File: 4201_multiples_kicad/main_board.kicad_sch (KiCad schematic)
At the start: 31 parts, among them J19 Conn_02x05_Odd_Even, U1 TL074, U2 TL074

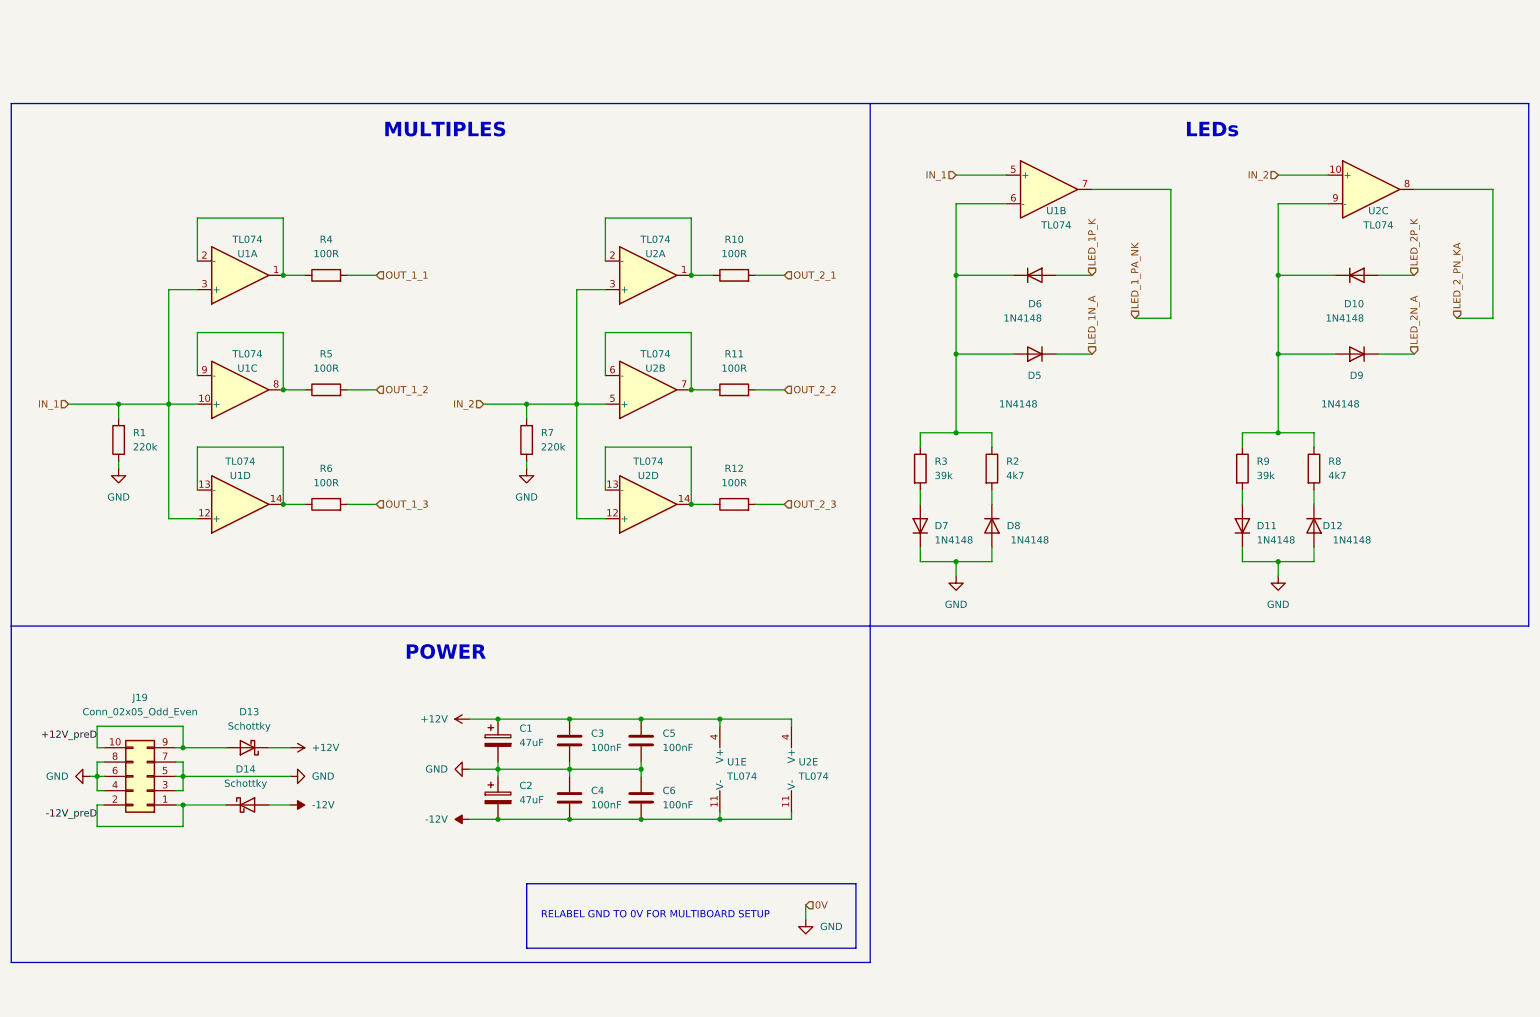
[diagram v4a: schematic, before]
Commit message: Update LED current limiting resistor values for equal brightness
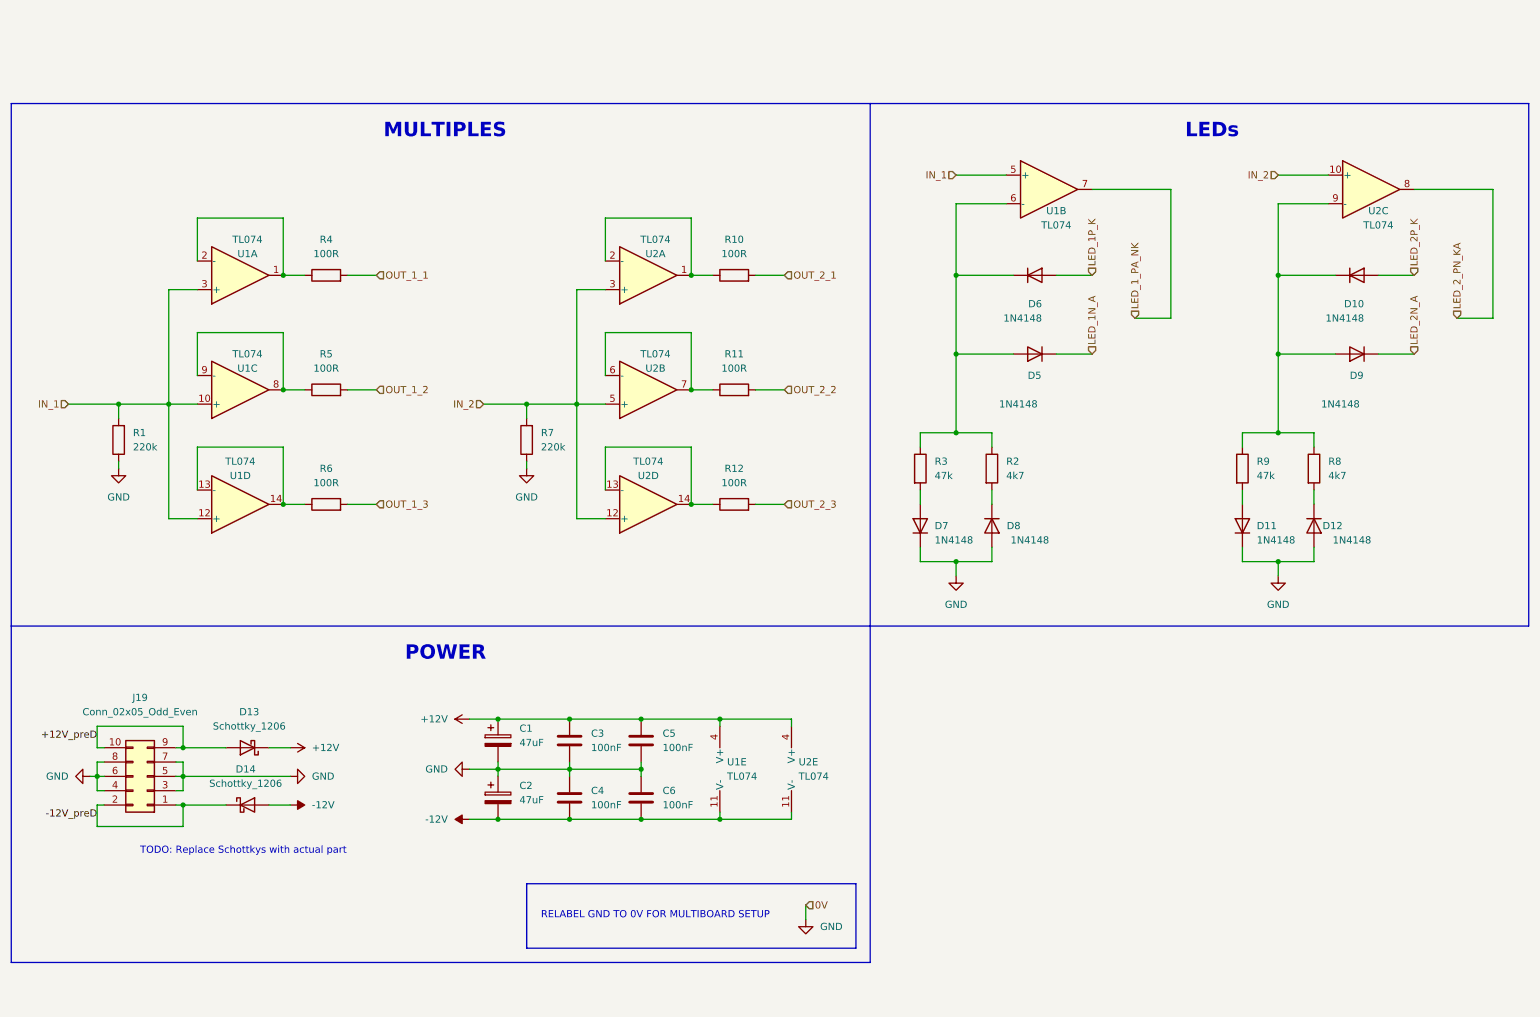
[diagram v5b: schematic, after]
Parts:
- D13, D14: value Schottky -> Schottky_1206
- R3, R9: value 39k -> 47k
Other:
- note added: "TODO: Replace Schottkys with actual part"
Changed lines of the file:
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@@
     (effects (font (size 2.54 2.54) bold) (justify left bottom))
+  )
+  (text "TODO: Replace Schottkys with actual part" (at 36.83 165.1 0)
+    (effects (font (size 1.27 1.27)) (justify left bottom))
   )
   (text "LEDs" (at 222.25 38.1 0)
@@
       (effects (font (size 1.27 1.27)) (justify left))
     )
-    (property "Value" "39k" (id 1) (at 177.8 97.7899 0)
+    (property "Value" "47k" (id 1) (at 177.8 97.7899 0)
       (effects (font (size 1.27 1.27)) (justify left))
     )
@@
     (in_bom yes) (on_board yes) (fields_autoplaced)
     (property "Reference" "D13" (id 0) (at 56.1975 139.7 0))
-    (property "Value" "Schottky" (id 1) (at 56.1975 142.24 0))
+    (property "Value" "Schottky_1206" (id 1) (at 56.1975 142.24 0))
     (property "Footprint" "Diode_SMD:D_1206_3216Metric_Pad1.42x1.75mm_HandSolder" (id 2) (at 55.88 141.605 0)
       (effects (font (size 1.27 1.27)) hide)
@@
       (effects (font (size 1.27 1.27)) (justify left))
     )
-    (property "Value" "39k" (id 1) (at 234.95 97.7899 0)
+    (property "Value" "47k" (id 1) (at 234.95 97.7899 0)
       (effects (font (size 1.27 1.27)) (justify left))
     )
@@
     (in_bom yes) (on_board yes) (fields_autoplaced)
     (property "Reference" "D14" (id 0) (at 55.5625 149.86 0))
-    (property "Value" "Schottky" (id 1) (at 55.5625 152.4 0))
+    (property "Value" "Schottky_1206" (id 1) (at 55.5625 152.4 0))
     (property "Footprint" "Diode_SMD:D_1206_3216Metric_Pad1.42x1.75mm_HandSolder" (id 2) (at 55.88 160.655 0)
       (effects (font (size 1.27 1.27)) hide)

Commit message: Set LED resistor values and change ICs to LM324
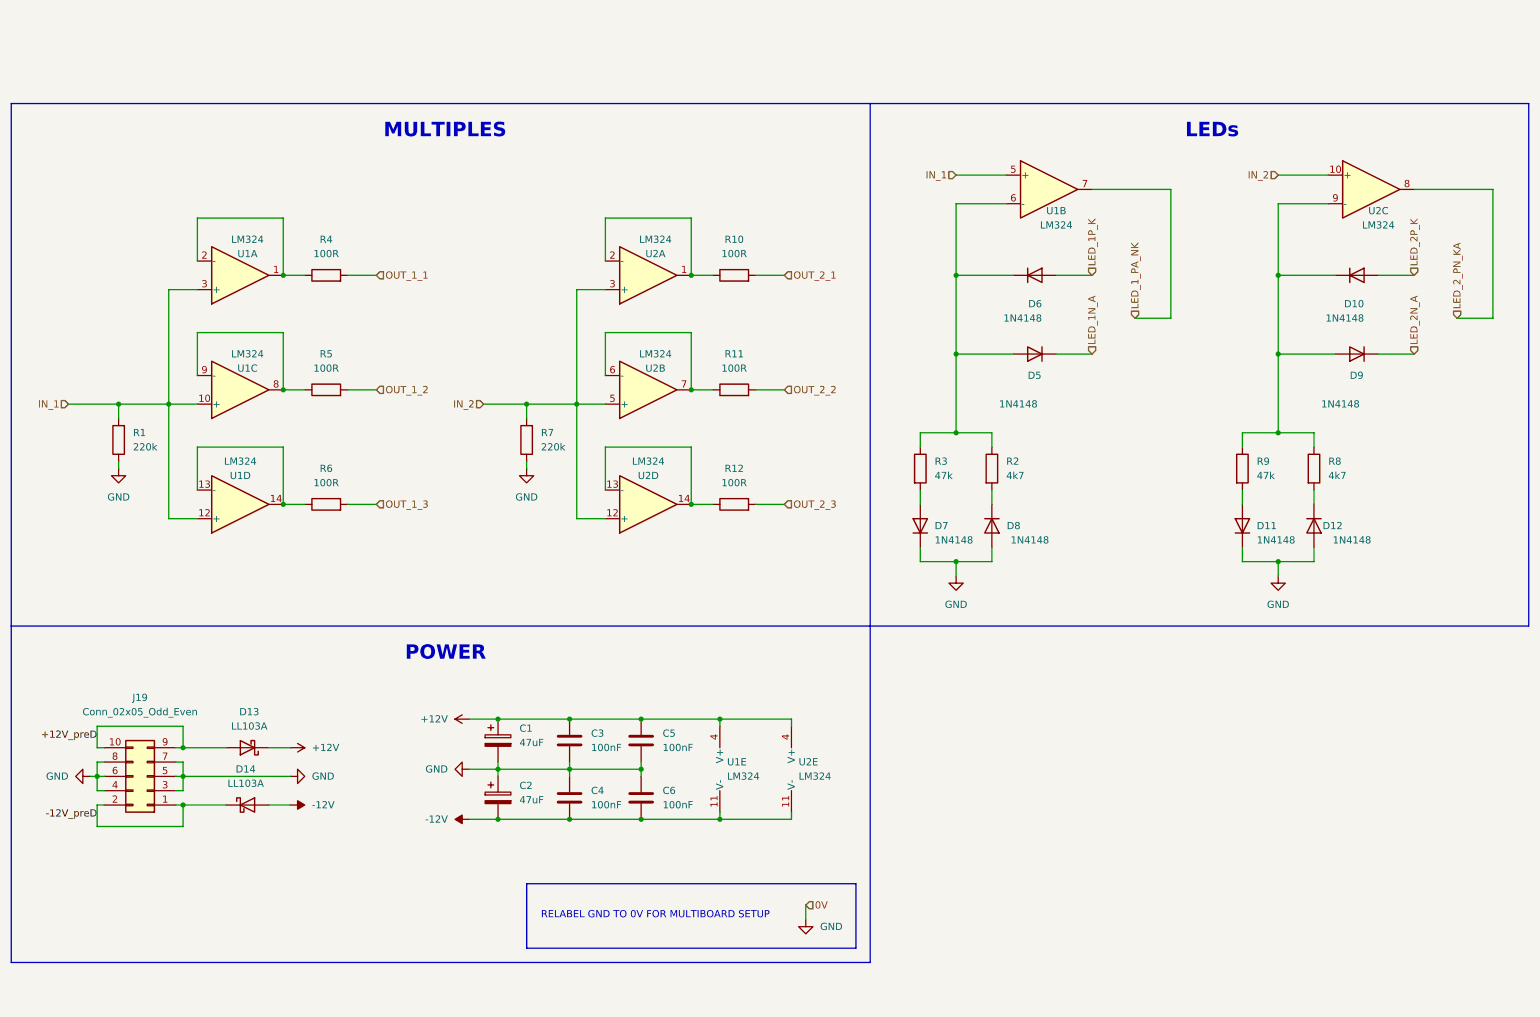
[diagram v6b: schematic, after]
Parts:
- D13, D14: value Schottky_1206 -> LL103A
- U1, U2: value TL074 -> LM324
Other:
- note removed: "TODO: Replace Schottkys with actual part"
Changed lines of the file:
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@@
     (effects (font (size 2.54 2.54) bold) (justify left bottom))
-  )
-  (text "TODO: Replace Schottkys with actual part" (at 36.83 165.1 0)
-    (effects (font (size 1.27 1.27)) (justify left bottom))
   )
   (text "LEDs" (at 222.25 38.1 0)
@@
       (effects (font (size 1.27 1.27)) (justify left))
     )
-    (property "Value" "TL074" (id 1) (at 153.67 151.1299 0)
+    (property "Value" "LM324" (id 1) (at 153.67 151.1299 0)
       (effects (font (size 1.27 1.27)) (justify left))
     )
@@
     (in_bom yes) (on_board yes)
     (property "Reference" "U2" (id 0) (at 128.27 78.74 0))
-    (property "Value" "TL074" (id 1) (at 128.27 76.2 0))
+    (property "Value" "LM324" (id 1) (at 128.27 76.2 0))
     (property "Footprint" "Package_SO:SOIC-14_3.9x8.7mm_P1.27mm" (id 2) (at 125.73 85.09 0)
       (effects (font (size 1.27 1.27)) hide)
@@
     (in_bom yes) (on_board yes)
     (property "Reference" "U1" (id 0) (at 55.88 78.74 0))
-    (property "Value" "TL074" (id 1) (at 55.88 76.2 0))
+    (property "Value" "LM324" (id 1) (at 55.88 76.2 0))
     (property "Footprint" "Package_SO:SOIC-14_3.9x8.7mm_P1.27mm" (id 2) (at 53.34 85.09 0)
       (effects (font (size 1.27 1.27)) hide)
@@
     (in_bom yes) (on_board yes)
     (property "Reference" "U1" (id 0) (at 55.88 58.42 0))
-    (property "Value" "TL074" (id 1) (at 55.88 55.88 0))
+    (property "Value" "LM324" (id 1) (at 55.88 55.88 0))
     (property "Footprint" "Package_SO:SOIC-14_3.9x8.7mm_P1.27mm" (id 2) (at 53.34 64.77 0)
       (effects (font (size 1.27 1.27)) hide)
@@
     (in_bom yes) (on_board yes) (fields_autoplaced)
     (property "Reference" "D13" (id 0) (at 56.1975 139.7 0))
-    (property "Value" "Schottky_1206" (id 1) (at 56.1975 142.24 0))
+    (property "Value" "LL103A" (id 1) (at 56.1975 142.24 0))
     (property "Footprint" "Diode_SMD:D_1206_3216Metric_Pad1.42x1.75mm_HandSolder" (id 2) (at 55.88 141.605 0)
       (effects (font (size 1.27 1.27)) hide)
@@
     (in_bom yes) (on_board yes)
     (property "Reference" "U1" (id 0) (at 199.39 50.8 0))
-    (property "Value" "TL074" (id 1) (at 199.39 53.34 0))
+    (property "Value" "LM324" (id 1) (at 199.39 53.34 0))
     (property "Footprint" "Package_SO:SOIC-14_3.9x8.7mm_P1.27mm" (id 2) (at 196.85 44.45 0)
       (effects (font (size 1.27 1.27)) hide)
@@
     (in_bom yes) (on_board yes)
     (property "Reference" "U2" (id 0) (at 127 97.79 0))
-    (property "Value" "TL074" (id 1) (at 127 95.25 0))
+    (property "Value" "LM324" (id 1) (at 127 95.25 0))
     (property "Footprint" "Package_SO:SOIC-14_3.9x8.7mm_P1.27mm" (id 2) (at 125.73 105.41 0)
       (effects (font (size 1.27 1.27)) hide)
@@
     (in_bom yes) (on_board yes)
     (property "Reference" "U2" (id 0) (at 128.27 58.42 0))
-    (property "Value" "TL074" (id 1) (at 128.27 55.88 0))
+    (property "Value" "LM324" (id 1) (at 128.27 55.88 0))
     (property "Footprint" "Package_SO:SOIC-14_3.9x8.7mm_P1.27mm" (id 2) (at 125.73 64.77 0)
       (effects (font (size 1.27 1.27)) hide)
@@
     (in_bom yes) (on_board yes)
     (property "Reference" "U2" (id 0) (at 256.54 50.8 0))
-    (property "Value" "TL074" (id 1) (at 256.54 53.34 0))
+    (property "Value" "LM324" (id 1) (at 256.54 53.34 0))
     (property "Footprint" "Package_SO:SOIC-14_3.9x8.7mm_P1.27mm" (id 2) (at 254 44.45 0)
       (effects (font (size 1.27 1.27)) hide)
@@
     (in_bom yes) (on_board yes)
     (property "Reference" "U1" (id 0) (at 54.61 97.79 0))
-    (property "Value" "TL074" (id 1) (at 54.61 95.25 0))
+    (property "Value" "LM324" (id 1) (at 54.61 95.25 0))
     (property "Footprint" "Package_SO:SOIC-14_3.9x8.7mm_P1.27mm" (id 2) (at 53.34 105.41 0)
       (effects (font (size 1.27 1.27)) hide)
@@
     (in_bom yes) (on_board yes) (fields_autoplaced)
     (property "Reference" "D14" (id 0) (at 55.5625 149.86 0))
-    (property "Value" "Schottky_1206" (id 1) (at 55.5625 152.4 0))
+    (property "Value" "LL103A" (id 1) (at 55.5625 152.4 0))
     (property "Footprint" "Diode_SMD:D_1206_3216Metric_Pad1.42x1.75mm_HandSolder" (id 2) (at 55.88 160.655 0)
       (effects (font (size 1.27 1.27)) hide)
@@
       (effects (font (size 1.27 1.27)) (justify left))
     )
-    (property "Value" "TL074" (id 1) (at 140.97 151.1299 0)
-      (effects (font (size 1.27 1.27)) (justify left))
-    )
+    (property "Value" "LM324" (id 1) (at 140.97 151.1299 0)
+      (effects (font (size 1.27 1.27)) (justify left))
+    )

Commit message: Update schematic
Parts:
- C1, C2: value 47uF -> 22u
- R1, R7: value 220k -> 470k
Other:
- note added: "High-end op-amp alternative: OPA4171 (If used, output resistors can be 51R)"
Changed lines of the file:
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@@
     (effects (font (size 2.54 2.54) bold) (justify left bottom))
+  )
+  (text "High-end op-amp alternative: OPA4171\n(If used, output resistors can be 51R)"
+    (at 16.51 121.92 0)
+    (effects (font (size 1.27 1.27)) (justify left bottom))
   )
   (text "LEDs" (at 222.25 38.1 0)
@@
       (effects (font (size 1.27 1.27)) (justify right))
     )
-    (property "Value" "220k" (id 1) (at 35.56 92.7099 0)
+    (property "Value" "470k" (id 1) (at 35.56 92.7099 0)
       (effects (font (size 1.27 1.27)) (justify right))
     )
@@
       (effects (font (size 1.27 1.27)) (justify right))
     )
-    (property "Value" "220k" (id 1) (at 107.95 92.7099 0)
+    (property "Value" "470k" (id 1) (at 107.95 92.7099 0)
       (effects (font (size 1.27 1.27)) (justify right))
     )
@@
       (effects (font (size 1.27 1.27)) (justify left))
     )
-    (property "Value" "47uF" (id 1) (at 104.14 145.1609 0)
+    (property "Value" "22u" (id 1) (at 104.14 145.1609 0)
       (effects (font (size 1.27 1.27)) (justify left))
     )
@@
       (effects (font (size 1.27 1.27)) (justify left))
     )
-    (property "Value" "47uF" (id 1) (at 104.14 155.3209 0)
-      (effects (font (size 1.27 1.27)) (justify left))
-    )
+    (property "Value" "22u" (id 1) (at 104.14 155.3209 0)
+      (effects (font (size 1.27 1.27)) (justify left))
+    )
